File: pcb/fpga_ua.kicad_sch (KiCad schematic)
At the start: 17 parts, among them U666 XC7A75T-FTG256, Y1101 ECS-2520MV-080-BN-TR

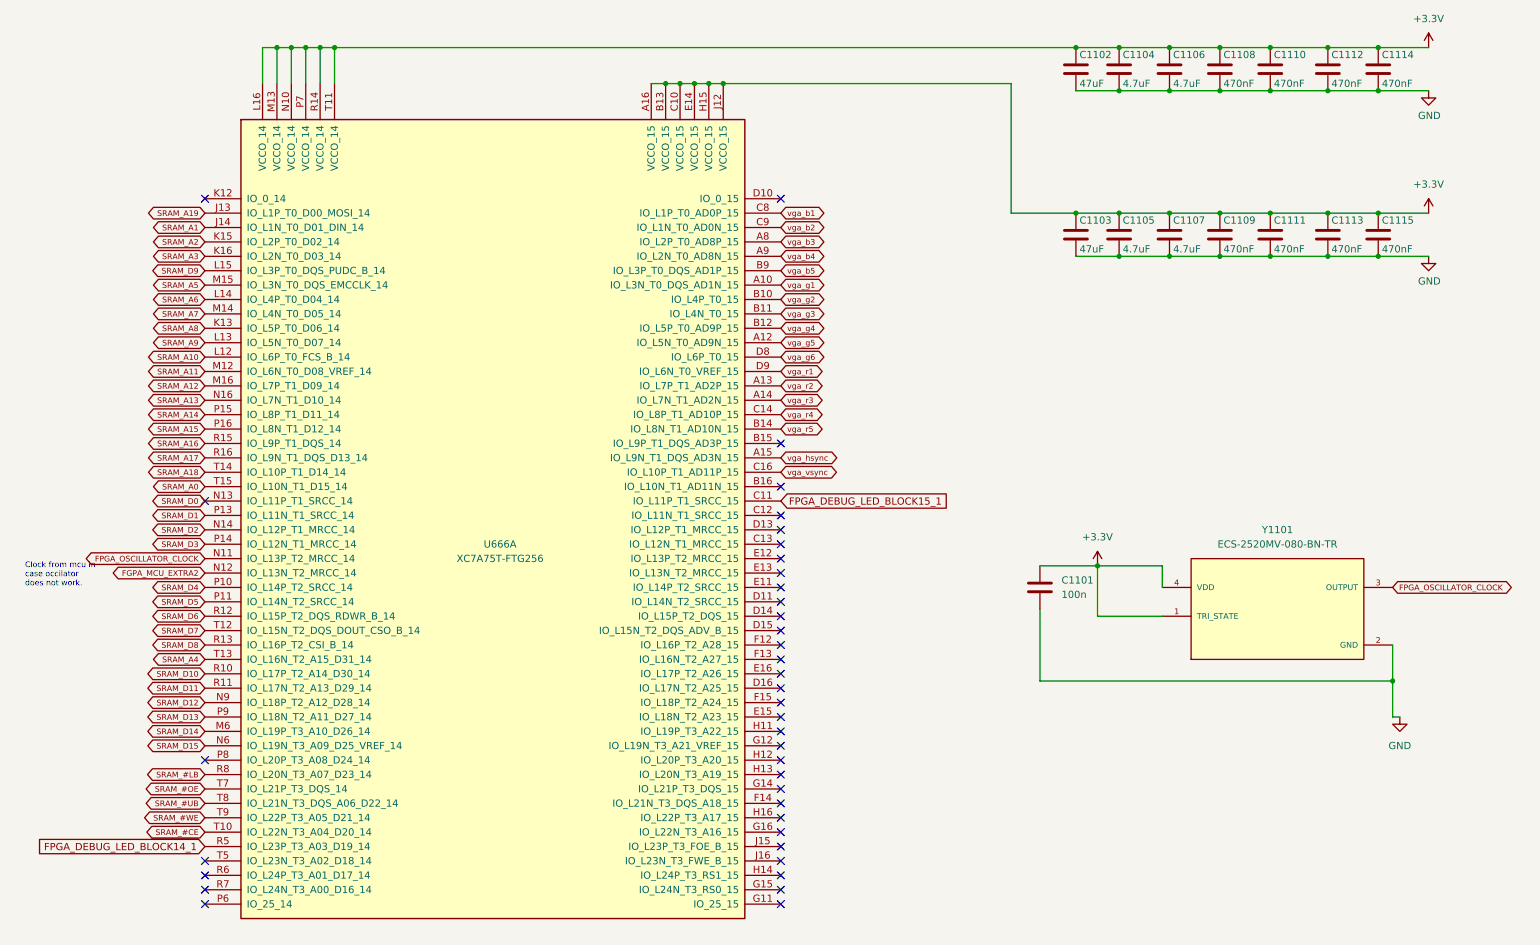
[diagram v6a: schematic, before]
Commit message: make lines between sram and fpga
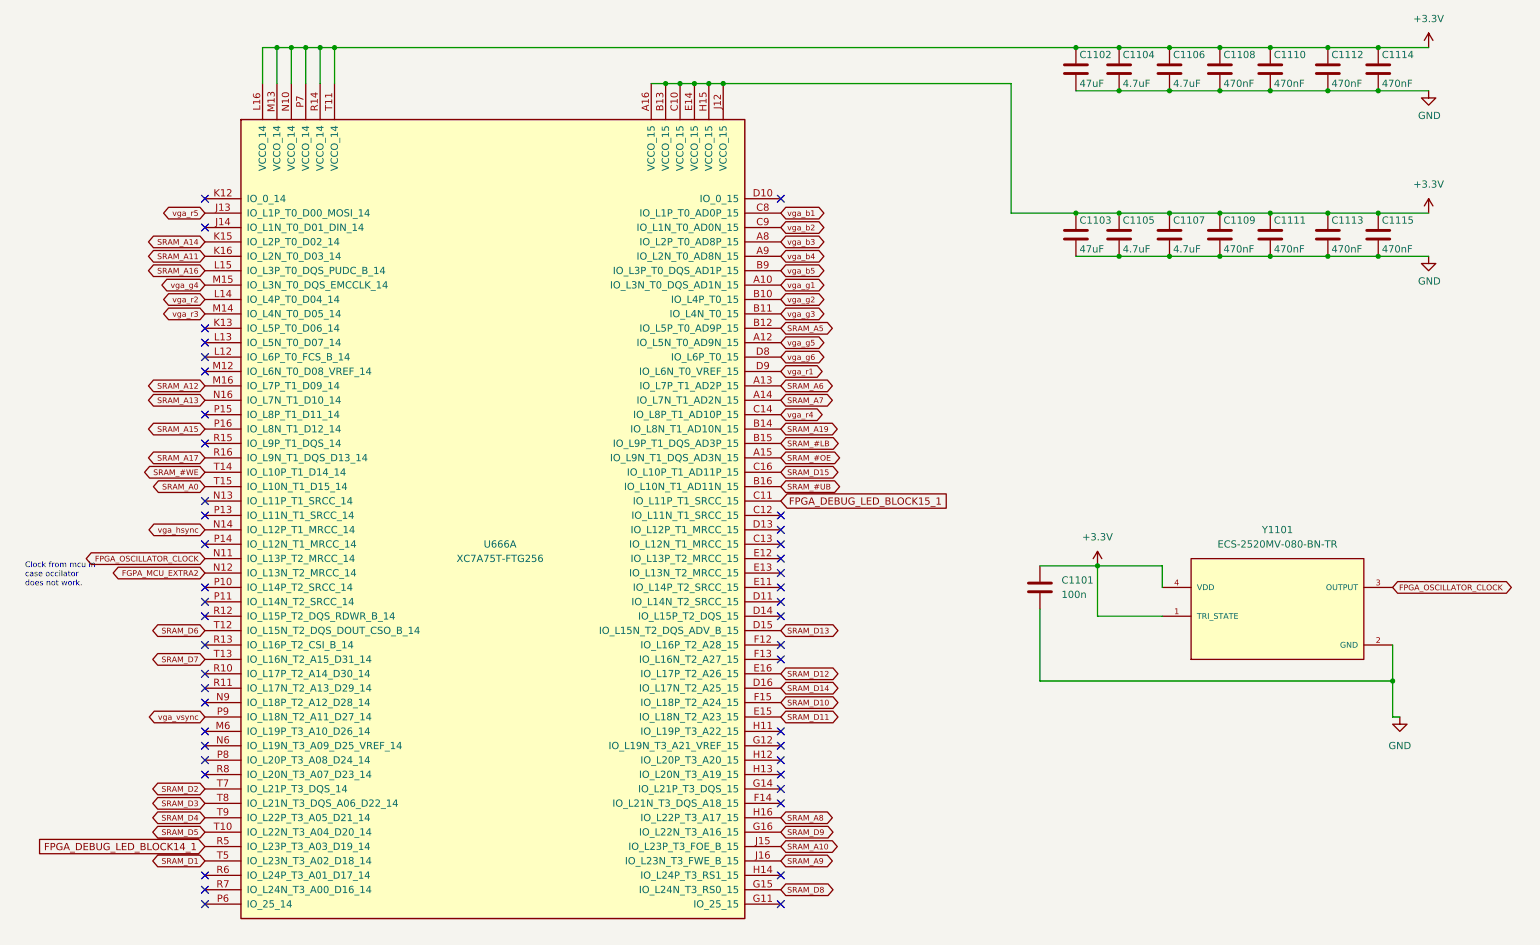
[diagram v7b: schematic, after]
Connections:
- net SRAM_#CE is gone; now on net SRAM_D5: U666.T10 (IO_L22N_T3_A04_D20_14)
- net SRAM_A18 is gone; now on net SRAM_#WE: U666.T14 (IO_L10P_T1_D14_14)
- net SRAM_A2 is gone; now on net SRAM_A14: U666.K15 (IO_L2P_T0_D02_14)
- net SRAM_A3 is gone; now on net SRAM_A11: U666.K16 (IO_L2N_T0_D03_14)
- net SRAM_A4 is gone; now on net SRAM_D7: U666.T13 (IO_L16N_T2_A15_D31_14)
- net SRAM_#LB: now also U666.B15 (IO_L9P_T1_DQS_AD3P_15); no longer U666.R8 (IO_L20N_T3_A07_D23_14)
- net SRAM_#OE: now also U666.A15 (IO_L9N_T1_DQS_AD3N_15); no longer U666.T7 (IO_L21P_T3_DQS_14)
- net SRAM_#UB: now also U666.B16 (IO_L10N_T1_AD11N_15); no longer U666.T8 (IO_L21N_T3_DQS_A06_D22_14)
- net SRAM_#WE: no longer U666.T9 (IO_L22P_T3_A05_D21_14)
- net SRAM_A10: now also U666.J15 (IO_L23P_T3_FOE_B_15); no longer U666.L12 (IO_L6P_T0_FCS_B_14)
- net SRAM_A11: no longer U666.M12 (IO_L6N_T0_D08_VREF_14)
- net SRAM_A14: no longer U666.P15 (IO_L8P_T1_D11_14)
- net SRAM_A16: now also U666.L15 (IO_L3P_T0_DQS_PUDC_B_14); no longer U666.R15 (IO_L9P_T1_DQS_14)
- net SRAM_A19: now also U666.B14 (IO_L8N_T1_AD10N_15); no longer U666.J13 (IO_L1P_T0_D00_MOSI_14)
- net SRAM_A5: now also U666.B12 (IO_L5P_T0_AD9P_15); no longer U666.M15 (IO_L3N_T0_DQS_EMCCLK_14)
- net SRAM_A6: now also U666.A13 (IO_L7P_T1_AD2P_15); no longer U666.L14 (IO_L4P_T0_D04_14)
- net SRAM_A7: now also U666.A14 (IO_L7N_T1_AD2N_15); no longer U666.M14 (IO_L4N_T0_D05_14)
- net SRAM_A8: now also U666.H16 (IO_L22P_T3_A17_15); no longer U666.K13 (IO_L5P_T0_D06_14)
- net SRAM_A9: now also U666.J16 (IO_L23N_T3_FWE_B_15); no longer U666.L13 (IO_L5N_T0_D07_14)
- net SRAM_D1: now also U666.T5 (IO_L23N_T3_A02_D18_14); no longer U666.P13 (IO_L11N_T1_SRCC_14)
- net SRAM_D10: now also U666.F15 (IO_L18P_T2_A24_15); no longer U666.R10 (IO_L17P_T2_A14_D30_14)
- net SRAM_D11: now also U666.E15 (IO_L18N_T2_A23_15); no longer U666.R11 (IO_L17N_T2_A13_D29_14)
- net SRAM_D12: now also U666.E16 (IO_L17P_T2_A26_15); no longer U666.N9 (IO_L18P_T2_A12_D28_14)
- net SRAM_D13: now also U666.D15 (IO_L15N_T2_DQS_ADV_B_15); no longer U666.P9 (IO_L18N_T2_A11_D27_14)
- net SRAM_D14: now also U666.D16 (IO_L17N_T2_A25_15); no longer U666.M6 (IO_L19P_T3_A10_D26_14)
- net SRAM_D15: now also U666.C16 (IO_L10P_T1_AD11P_15); no longer U666.N6 (IO_L19N_T3_A09_D25_VREF_14)
- net SRAM_D2: now also U666.T7 (IO_L21P_T3_DQS_14); no longer U666.N14 (IO_L12P_T1_MRCC_14)
- net SRAM_D3: now also U666.T8 (IO_L21N_T3_DQS_A06_D22_14); no longer U666.P14 (IO_L12N_T1_MRCC_14)
- net SRAM_D4: now also U666.T9 (IO_L22P_T3_A05_D21_14); no longer U666.P10 (IO_L14P_T2_SRCC_14)
- net SRAM_D5: no longer U666.P11 (IO_L14N_T2_SRCC_14)
- net SRAM_D6: now also U666.T12 (IO_L15N_T2_DQS_DOUT_CSO_B_14); no longer U666.R12 (IO_L15P_T2_DQS_RDWR_B_14)
- net SRAM_D7: no longer U666.T12 (IO_L15N_T2_DQS_DOUT_CSO_B_14)
- net SRAM_D8: now also U666.G15 (IO_L24N_T3_RS0_15); no longer U666.R13 (IO_L16P_T2_CSI_B_14)
- net SRAM_D9: now also U666.G16 (IO_L22N_T3_A16_15); no longer U666.L15 (IO_L3P_T0_DQS_PUDC_B_14)
- net vga_g4: now also U666.M15 (IO_L3N_T0_DQS_EMCCLK_14); no longer U666.B12 (IO_L5P_T0_AD9P_15)
- net vga_hsync: now also U666.N14 (IO_L12P_T1_MRCC_14); no longer U666.A15 (IO_L9N_T1_DQS_AD3N_15)
- net vga_r2: now also U666.L14 (IO_L4P_T0_D04_14); no longer U666.A13 (IO_L7P_T1_AD2P_15)
- net vga_r3: now also U666.M14 (IO_L4N_T0_D05_14); no longer U666.A14 (IO_L7N_T1_AD2N_15)
- net vga_r5: now also U666.J13 (IO_L1P_T0_D00_MOSI_14); no longer U666.B14 (IO_L8N_T1_AD10N_15)
- net vga_vsync: now also U666.P9 (IO_L18N_T2_A11_D27_14); no longer U666.C16 (IO_L10P_T1_AD11P_15)
- net SRAM_A1: no longer names the net of U666.J14 (IO_L1N_T0_D01_DIN_14)
- net SRAM_D0: no longer names the net of U666.N13 (IO_L11P_T1_SRCC_14)
- no-connect marks 38 -> 44

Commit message: vga is live
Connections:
- net vga_g1 is gone; now on net vga_b2: U666.A10 (IO_L3N_T0_DQS_AD1N_15)
- net vga_g2 is gone; now on net vga_b1: U666.B10 (IO_L4P_T0_15)
- net vga_g3 is gone; now on net vga_vsync: U666.B11 (IO_L4N_T0_15)
- net vga_g5 is gone; now on net vga_hsync: U666.A12 (IO_L5N_T0_AD9N_15)
- net FPGA_OSCILLATOR_CLOCK: now also U666.P14 (IO_L12N_T1_MRCC_14); no longer U666.N11 (IO_L13P_T2_MRCC_14)
- net vga_b1: no longer U666.C8 (IO_L1P_T0_AD0P_15)
- net vga_b2: no longer U666.C9 (IO_L1N_T0_AD0N_15)
- net vga_b3: now also U666.B9 (IO_L3P_T0_DQS_AD1P_15); no longer U666.A8 (IO_L2P_T0_AD8P_15)
- net vga_b5: now also U666.A8 (IO_L2P_T0_AD8P_15); no longer U666.B9 (IO_L3P_T0_DQS_AD1P_15)
- net vga_hsync: no longer U666.N14 (IO_L12P_T1_MRCC_14)
- net vga_vsync: no longer U666.P9 (IO_L18N_T2_A11_D27_14)
- net vga_g4: no longer names the net of U666.M15 (IO_L3N_T0_DQS_EMCCLK_14)
- net vga_g6 renamed FPGA_GPIO_8
- net vga_r1: no longer names the net of U666.D9 (IO_L6N_T0_VREF_15)
- net vga_r2 renamed FPGA_GPIO_9
- net vga_r3: no longer names the net of U666.M14 (IO_L4N_T0_D05_14)
- net vga_r4 renamed FPGA_GPIO_1
- net vga_r5: no longer names the net of U666.J13 (IO_L1P_T0_D00_MOSI_14)
- new net FPGA_GPIO_10: U666.C9 (IO_L1N_T0_AD0N_15)
- new net FPGA_GPIO_11: U666.P9 (IO_L18N_T2_A11_D27_14)
- new net FPGA_GPIO_7: U666.C8 (IO_L1P_T0_AD0P_15)
- no-connect marks 44 -> 49
